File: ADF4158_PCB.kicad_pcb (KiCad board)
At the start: 4 copper layers, 55 x 25 mm, 83 parts, among them J1 Conn_02x04_Odd_Even, J2 SMA, J3 SMA, Q1 DMP3099L-13, Q2 2N7002BK, U1 LP2985-10.0, U2 TLV74130P, U3 TLV74033P, U4 HMC391, U5 AD8065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

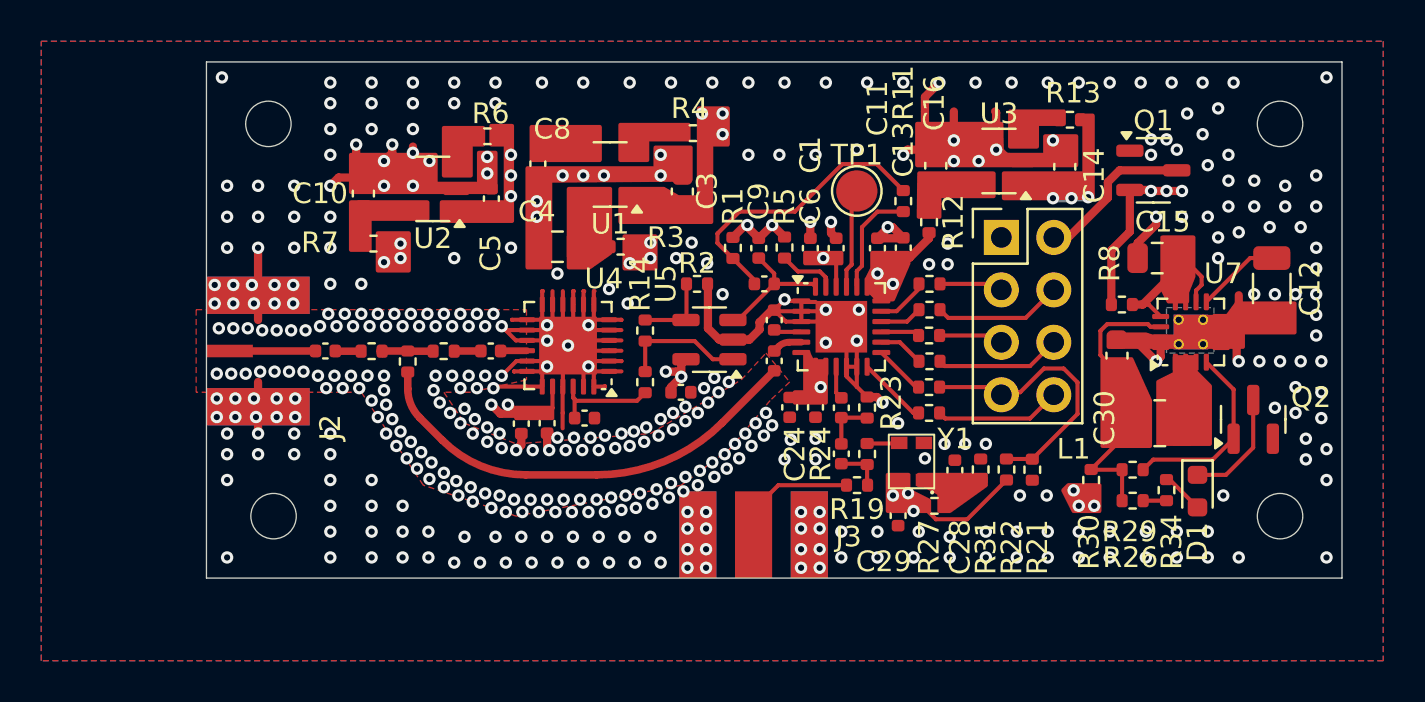
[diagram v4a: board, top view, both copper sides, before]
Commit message: add plating to mounting holes
Signed-off-by: Daniel Estévez <daniel@destevez.net>
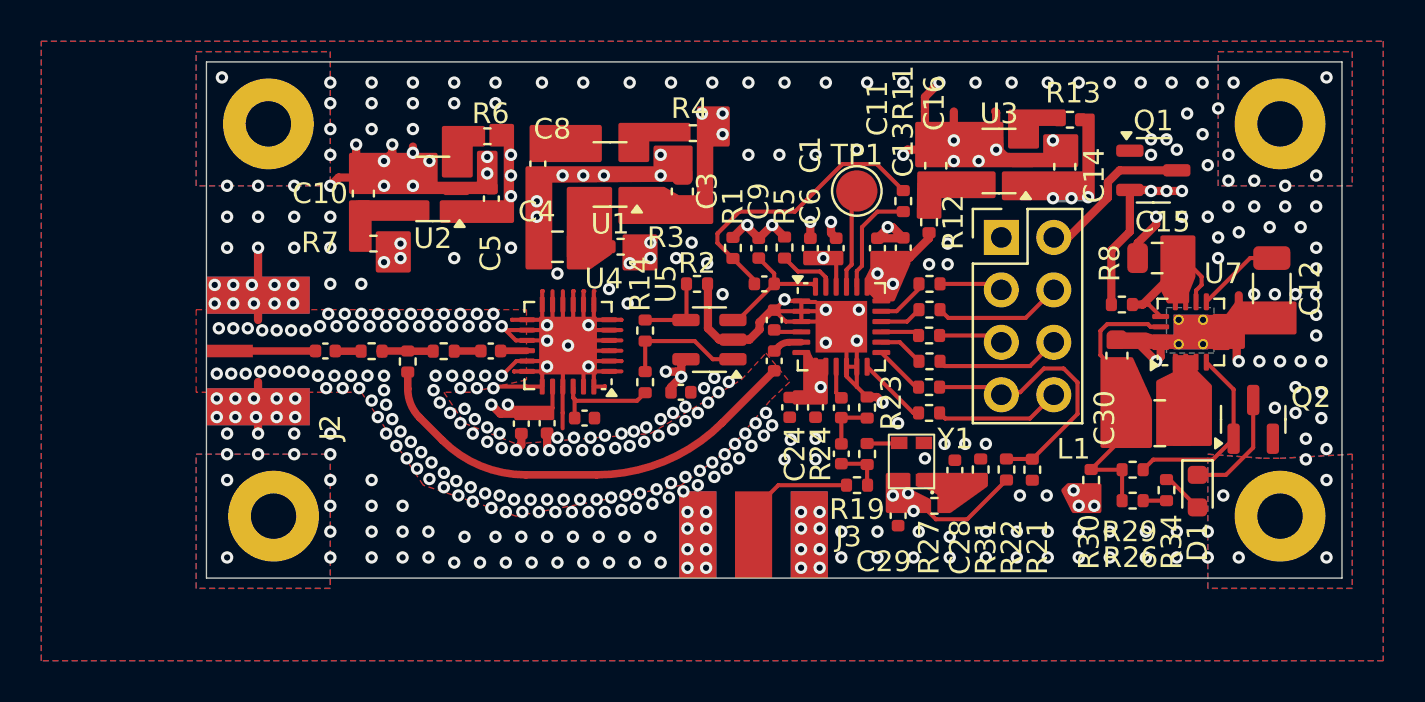
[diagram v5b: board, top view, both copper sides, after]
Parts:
- H1, H2, H3, H4: footprint MountingHole:MountingHole_2.2mm_M2 -> MountingHole:MountingHole_2.2mm_M2_Pad
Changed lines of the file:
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@@
 		)
 	)
-	(footprint "MountingHole:MountingHole_2.2mm_M2"
+	(footprint "MountingHole:MountingHole_2.2mm_M2_Pad"
 		(layer "F.Cu")
 		(at 125.5 91)
-		(descr "Mounting Hole 2.2mm, no annular, M2")
-		(tags "mounting hole 2.2mm no annular m2")
+		(descr "Mounting Hole 2.2mm, M2")
+		(tags "mounting hole 2.2mm m2")
 		(property "Reference" "H1"
 			(at 0 -3.2 0)
@@
 			)
 		)
-		(property "Description" "Mounting Hole without connection"
+		(property "Description" "Mounting Hole with connection"
 			(at 0 0 0)
 			(unlocked yes)
@@
 			)
 		)
-		(property ki_fp_filters "MountingHole*")
+		(property ki_fp_filters "MountingHole*Pad*")
 		(sheetname "/Connectors/")
 		(sheetfile "connectors.kicad_sch")
@@
 			)
 		)
-		(pad "" np_thru_hole circle
+		(pad "1" thru_hole circle
 			(at 0 0)
-			(size 2.2 2.2)
+			(size 4.4 4.4)
 			(drill 2.2)
 			(layers "*.Cu" "*.Mask")
+			(remove_unused_layers no)
+			(net 2 "GND")
+			(pinfunction "1")
+			(pintype "input")
 		)
 		(embedded_fonts no)
@@
 		)
 	)
-	(footprint "MountingHole:MountingHole_2.2mm_M2"
+	(footprint "MountingHole:MountingHole_2.2mm_M2_Pad"
 		(layer "F.Cu")
 		(at 125.75 110)
-		(descr "Mounting Hole 2.2mm, no annular, M2")
-		(tags "mounting hole 2.2mm no annular m2")
+		(descr "Mounting Hole 2.2mm, M2")
+		(tags "mounting hole 2.2mm m2")
 		(property "Reference" "H3"
 			(at 0 -3.2 0)
@@
 			)
 		)
-		(property "Description" "Mounting Hole without connection"
+		(property "Description" "Mounting Hole with connection"
 			(at 0 0 0)
 			(unlocked yes)
@@
 			)
 		)
-		(property ki_fp_filters "MountingHole*")
+		(property ki_fp_filters "MountingHole*Pad*")
 		(sheetname "/Connectors/")
 		(sheetfile "connectors.kicad_sch")
@@
 			)
 		)
-		(pad "" np_thru_hole circle
+		(pad "1" thru_hole circle
 			(at 0 0)
-			(size 2.2 2.2)
+			(size 4.4 4.4)
 			(drill 2.2)
 			(layers "*.Cu" "*.Mask")
+			(remove_unused_layers no)
+			(net 2 "GND")
+			(pinfunction "1")
+			(pintype "input")
 		)
 		(embedded_fonts no)
@@
 		)
 	)
-	(footprint "MountingHole:MountingHole_2.2mm_M2"
+	(footprint "MountingHole:MountingHole_2.2mm_M2_Pad"
 		(layer "F.Cu")
 		(at 174.5 91)
-		(descr "Mounting Hole 2.2mm, no annular, M2")
-		(tags "mounting hole 2.2mm no annular m2")
+		(descr "Mounting Hole 2.2mm, M2")
+		(tags "mounting hole 2.2mm m2")
 		(property "Reference" "H2"
 			(at 0 -3.2 0)
@@
 			)
 		)
-		(property "Description" "Mounting Hole without connection"
+		(property "Description" "Mounting Hole with connection"
 			(at 0 0 0)
 			(unlocked yes)
@@
 			)
 		)
-		(property ki_fp_filters "MountingHole*")
+		(property ki_fp_filters "MountingHole*Pad*")
 		(sheetname "/Connectors/")
 		(sheetfile "connectors.kicad_sch")
@@
 			)
 		)
-		(pad "" np_thru_hole circle
+		(pad "1" thru_hole circle
 			(at 0 0)
-			(size 2.2 2.2)
+			(size 4.4 4.4)
 			(drill 2.2)
 			(layers "*.Cu" "*.Mask")
+			(remove_unused_layers no)
+			(net 2 "GND")
+			(pinfunction "1")
+			(pintype "input")
 		)
 		(embedded_fonts no)
@@
 		)
 	)
-	(footprint "MountingHole:MountingHole_2.2mm_M2"
+	(footprint "MountingHole:MountingHole_2.2mm_M2_Pad"
 		(layer "F.Cu")
 		(at 174.5 110)
-		(descr "Mounting Hole 2.2mm, no annular, M2")
-		(tags "mounting hole 2.2mm no annular m2")
+		(descr "Mounting Hole 2.2mm, M2")
+		(tags "mounting hole 2.2mm m2")
 		(property "Reference" "H4"
 			(at 0 -3.2 0)
@@
 			)
 		)
-		(property "Description" "Mounting Hole without connection"
+		(property "Description" "Mounting Hole with connection"
 			(at 0 0 0)
 			(unlocked yes)
@@
 			)
 		)
-		(property ki_fp_filters "MountingHole*")
+		(property ki_fp_filters "MountingHole*Pad*")
 		(sheetname "/Connectors/")
 		(sheetfile "connectors.kicad_sch")
@@
 			)
 		)
-		(pad "" np_thru_hole circle
+		(pad "1" thru_hole circle
 			(at 0 0)
-			(size 2.2 2.2)
+			(size 4.4 4.4)
 			(drill 2.2)
 			(layers "*.Cu" "*.Mask")
+			(remove_unused_layers no)
+			(net 2 "GND")
+			(pinfunction "1")
+			(pintype "input")
 		)
 		(embedded_fonts no)
@@
 			)
 		)
+	)
+	(zone
+		(net 2)
+		(net_name "GND")
+		(layers "F.Cu" "B.Cu" "In1.Cu" "In2.Cu")
+		(hatch edge 0.5)
+		(priority 8)
+		(connect_pads yes
+			(clearance 0.5)
+		)
+		(min_thickness 0.25)
+		(filled_areas_thickness no)
+		(fill yes
+			(thermal_gap 0.5)
+			(thermal_bridge_width 0.5)
+		)
+		(polygon
+			(pts
+				(xy 122 87.5) (xy 128.5 87.5) (xy 128.5 94) (xy 122 94)
+			)
+		)
+	)
+	(zone
+		(net 2)
+		(net_name "GND")
+		(layers "F.Cu" "B.Cu" "In1.Cu" "In2.Cu")
+		(hatch edge 0.5)
+		(priority 8)
+		(connect_pads yes
+			(clearance 0.5)
+		)
+		(min_thickness 0.25)
+		(filled_areas_thickness no)
+		(fill yes
+			(thermal_gap 0.5)
+			(thermal_bridge_width 0.5)
+		)
+		(polygon
+			(pts
+				(xy 122 107) (xy 128.5 107) (xy 128.5 113.5) (xy 122 113.5)
+			)
+		)
+	)
+	(zone
+		(net 2)
+		(net_name "GND")
+		(layers "F.Cu" "B.Cu" "In1.Cu" "In2.Cu")
+		(hatch edge 0.5)
+		(priority 8)
+		(connect_pads yes
+			(clearance 0.5)
+		)
+		(min_thickness 0.25)
+		(filled_areas_thickness no)
+		(fill yes
+			(thermal_gap 0.5)
+			(thermal_bridge_width 0.5)
+		)
+		(polygon
+			(pts
+				(xy 171 107) (xy 173.7 107.2) (xy 174.5 107.2) (xy 178 107) (xy 178 113.5) (xy 171 113.5)
+			)
+		)
+	)
+	(zone
+		(net 2)
+		(net_name "GND")
+		(layers "F.Cu" "B.Cu" "In1.Cu" "In2.Cu")
+		(hatch edge 0.5)
+		(priority 8)
+		(connect_pads yes
+			(clearance 0.5)
+		)
+		(min_thickness 0.25)
+		(filled_areas_thickness no)
+		(fill yes
+			(thermal_gap 0.5)
+			(thermal_bridge_width 0.5)
+		)
+		(polygon
+			(pts
+				(xy 171.5 87.5) (xy 178 87.5) (xy 178 94) (xy 171.5 94)
+			)
+		)

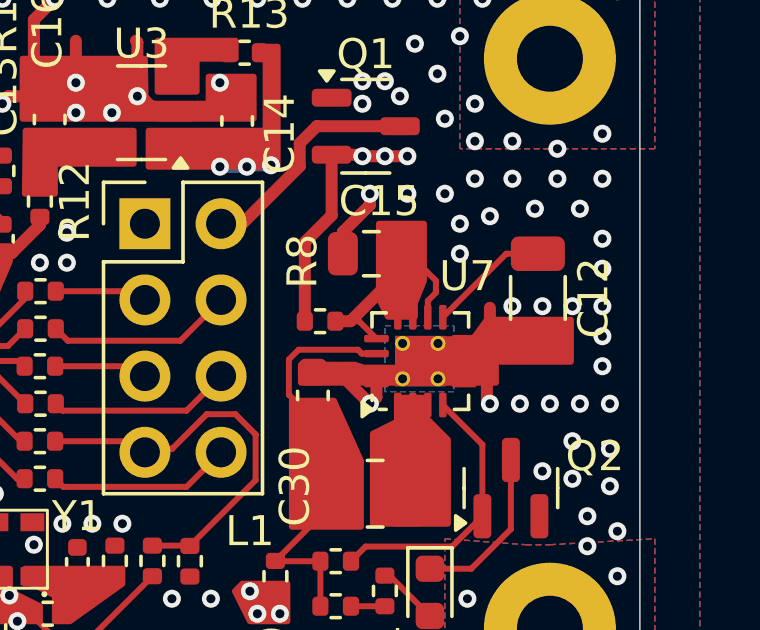
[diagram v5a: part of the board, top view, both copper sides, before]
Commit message: replace U7 footprint vias by manually placed vias
The thermal vias in the footprint were being connected
to the groundplane with thermal reliefs and giving other
troubles (wrong drill size). This replaces them by manually
placed vias.

Signed-off-by: Daniel Estévez <daniel@destevez.net>
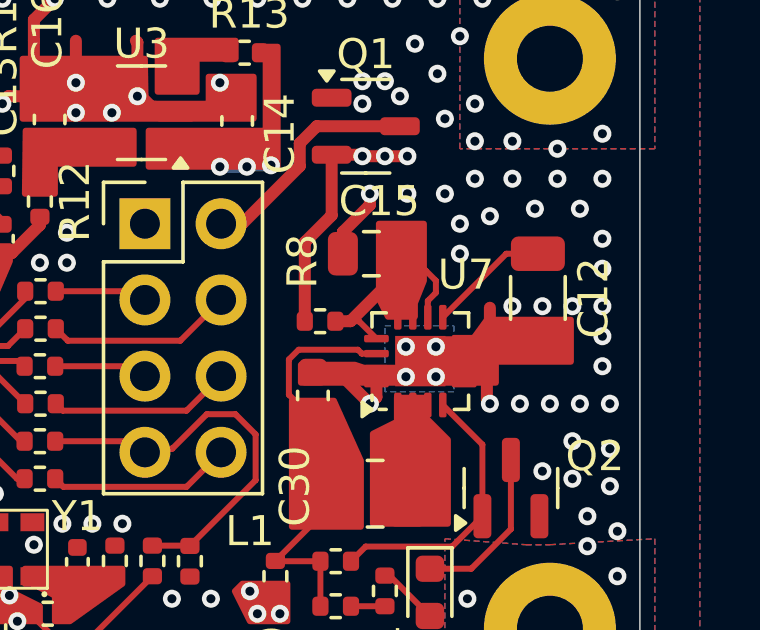
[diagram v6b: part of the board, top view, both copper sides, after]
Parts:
- U7: footprint Package_DFN_QFN:VQFN-16-1EP_3x3mm_P0.5mm_EP1.68x1.68mm_ThermalVias -> Package_DFN_QFN:VQFN-16-1EP_3x3mm_P0.5mm_EP1.68x1.68mm
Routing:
- net GND: vias 420 -> 424
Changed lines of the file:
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@@
 		)
 	)
-	(footprint "Package_DFN_QFN:VQFN-16-1EP_3x3mm_P0.5mm_EP1.68x1.68mm_ThermalVias"
+	(footprint "Package_DFN_QFN:VQFN-16-1EP_3x3mm_P0.5mm_EP1.68x1.68mm"
 		(layer "F.Cu")
 		(at 170.18 101.08 90)
@@
 		(tags "VQFN NoLead")
 		(property "Reference" "U7"
-			(at 2.83 1.57 180)
+			(at 2.88 1.52 180)
 			(layer "F.SilkS")
 			(effects
@@
 		)
 		(property "Value" "TPS62143"
-			(at 5.33 1.82 270)
+			(at 0 2.83 90)
 			(layer "F.Fab")
 			(effects
@@
 		)
 		(fp_text user "${REFERENCE}"
-			(at -1.67 -1.68 90)
+			(at 0 0 90)
 			(layer "F.Fab")
 			(effects
@@
 		(pad "" smd roundrect
 			(at -0.42 -0.42 90)
-			(size 0.73 0.73)
+			(size 0.68 0.68)
 			(layers "F.Paste")
 			(roundrect_rratio 0.25)
@@
 		(pad "" smd roundrect
 			(at -0.42 0.42 90)
-			(size 0.73 0.73)
+			(size 0.68 0.68)
 			(layers "F.Paste")
 			(roundrect_rratio 0.25)
@@
 		(pad "" smd roundrect
 			(at 0.42 -0.42 90)
-			(size 0.73 0.73)
+			(size 0.68 0.68)
 			(layers "F.Paste")
 			(roundrect_rratio 0.25)
@@
 		(pad "" smd roundrect
 			(at 0.42 0.42 90)
-			(size 0.73 0.73)
+			(size 0.68 0.68)
 			(layers "F.Paste")
 			(roundrect_rratio 0.25)
@@
 			(pintype "passive")
 		)
-		(pad "17" thru_hole circle
-			(at -0.59 -0.59 90)
-			(size 0.5 0.5)
-			(drill 0.3)
-			(property pad_prop_heatsink)
-			(layers "*.Cu")
-			(remove_unused_layers no)
-			(net 2 "GND")
-			(pinfunction "GND")
-			(pintype "passive")
-		)
-		(pad "17" thru_hole circle
-			(at -0.59 0.59 90)
-			(size 0.5 0.5)
-			(drill 0.3)
-			(property pad_prop_heatsink)
-			(layers "*.Cu")
-			(remove_unused_layers no)
-			(net 2 "GND")
-			(pinfunction "GND")
-			(pintype "passive")
-		)
 		(pad "17" smd rect
 			(at 0 0 90)
@@
 			(zone_connect 2)
 		)
-		(pad "17" smd rect
-			(at 0 0 90)
-			(size 1.68 1.68)
-			(property pad_prop_heatsink)
-			(layers "B.Cu")
-			(net 2 "GND")
-			(pinfunction "GND")
-			(pintype "passive")
-			(zone_connect 2)
-		)
-		(pad "17" thru_hole circle
-			(at 0.59 -0.59 90)
-			(size 0.5 0.5)
-			(drill 0.3)
-			(property pad_prop_heatsink)
-			(layers "*.Cu")
-			(remove_unused_layers no)
-			(net 2 "GND")
-			(pinfunction "GND")
-			(pintype "passive")
-		)
-		(pad "17" thru_hole circle
-			(at 0.59 0.59 90)
-			(size 0.5 0.5)
-			(drill 0.3)
-			(property pad_prop_heatsink)
-			(layers "*.Cu")
-			(remove_unused_layers no)
-			(net 2 "GND")
-			(pinfunction "GND")
-			(pintype "passive")
-		)
 		(embedded_fonts no)
 		(model "${KICAD9_3DMODEL_DIR}/Package_DFN_QFN.3dshapes/VQFN-16-1EP_3x3mm_P0.5mm_EP1.68x1.68mm.wrl"
@@
 	)
 	(via
+		(at 169.7 101.6)
+		(size 0.6)
+		(drill 0.3)
+		(layers "F.Cu" "B.Cu")
+		(net 2)
+	)
+	(via
 		(at 123 105.2)
 		(size 0.6)
@@
 	)
 	(via
+		(at 170.7 101.6)
+		(size 0.6)
+		(drill 0.3)
+		(layers "F.Cu" "B.Cu")
+		(net 2)
+	)
+	(via
 		(at 136.4 103.8)
 		(size 0.6)
@@
 	)
 	(via
+		(at 170.7 100.6)
+		(size 0.6)
+		(drill 0.3)
+		(layers "F.Cu" "B.Cu")
+		(net 2)
+	)
+	(via
 		(at 166.25 112)
 		(size 0.6)
@@
 	)
 	(via
+		(at 169.7 100.6)
+		(size 0.6)
+		(drill 0.3)
+		(layers "F.Cu" "B.Cu")
+		(net 2)
+	)
+	(via
 		(at 174.25 99.25)
 		(size 0.6)
@@
 	)
 	(zone
-		(net 2)
-		(net_name "GND")
+		(net 16)
+		(net_name "/rf_out")
 		(layer "F.Cu")
-		(hatch edge 0.5)
-		(priority 6)
-		(connect_pads
-			(clearance 0.5)
+		(name "$teardrop_padvia$")
+		(hatch full 0.1)
+		(priority 30000)
+		(attr
+			(teardrop
+				(type padvia)
+			)
 		)
-		(min_thickness 0.25)
+		(connect_pads yes
+			(clearance 0)
+		)
+		(min_thickness 0.0254)
 		(filled_areas_thickness no)
 		(fill yes
@@
 		(polygon
 			(pts
-				(xy 122 100) (xy 138 100) (xy 138 103.4) (xy 135.3 104) (xy 134 104) (xy 135 105.5) (xy 137.5 106.5)
-				(xy 144 106) (xy 148.4 103.4) (xy 149.6 102.1) (xy 150.75 103.5) (xy 149.8 104.4) (xy 147.9 106.7)
-				(xy 145.5 108.5) (xy 137.5 110) (xy 133 108.5) (xy 130 104) (xy 122 104)
+				(xy 125.055 102.1829) (xy 125.055 101.8171) (xy 124.75 101.695) (xy 123.624 102) (xy 124.75 102.305)
 			)
 		)
 	)
 	(zone
-		(net 16)
-		(net_name "/rf_out")
+		(net 2)
+		(net_name "GND")
 		(layer "F.Cu")
-		(name "$teardrop_padvia$")
-		(hatch full 0.1)
-		(priority 30000)
-		(attr
-			(teardrop
-				(type padvia)
-			)
-		)
-		(connect_pads yes
-			(clearance 0)
+		(hatch edge 0.5)
+		(priority 6)
+		(connect_pads
+			(clearance 0.5)
 		)
-		(min_thickness 0.0254)
+		(min_thickness 0.25)
 		(filled_areas_thickness no)
 		(fill yes
@@
 		(polygon
 			(pts
-				(xy 125.055 102.1829) (xy 125.055 101.8171) (xy 124.75 101.695) (xy 123.624 102) (xy 124.75 102.305)
+				(xy 122 100) (xy 138 100) (xy 138 103.4) (xy 135.3 104) (xy 134 104) (xy 135 105.5) (xy 137.5 106.5)
+				(xy 144 106) (xy 148.4 103.4) (xy 149.6 102.1) (xy 150.75 103.5) (xy 149.8 104.4) (xy 147.9 106.7)
+				(xy 145.5 108.5) (xy 137.5 110) (xy 133 108.5) (xy 130 104) (xy 122 104)
 			)
 		)
